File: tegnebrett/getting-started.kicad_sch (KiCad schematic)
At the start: 55 parts, among them J1 FH12-45S-0.5SH55, J2 FH12-6S-1SH55, J3 Conn_ST_STDC14, J5 MCU_Header_Pin, J7 USB_A, SW1 SW_Push, SW2 SW_Push, SW3 SW_Push, SW4 SW_Push, SW5 SW_Push, SW6 SW_Push, SW7 SW_Push, SW8 SW_Push, SW9 SW_Push, U5 STM32U5G7VJTxQ, Y1 60MHz

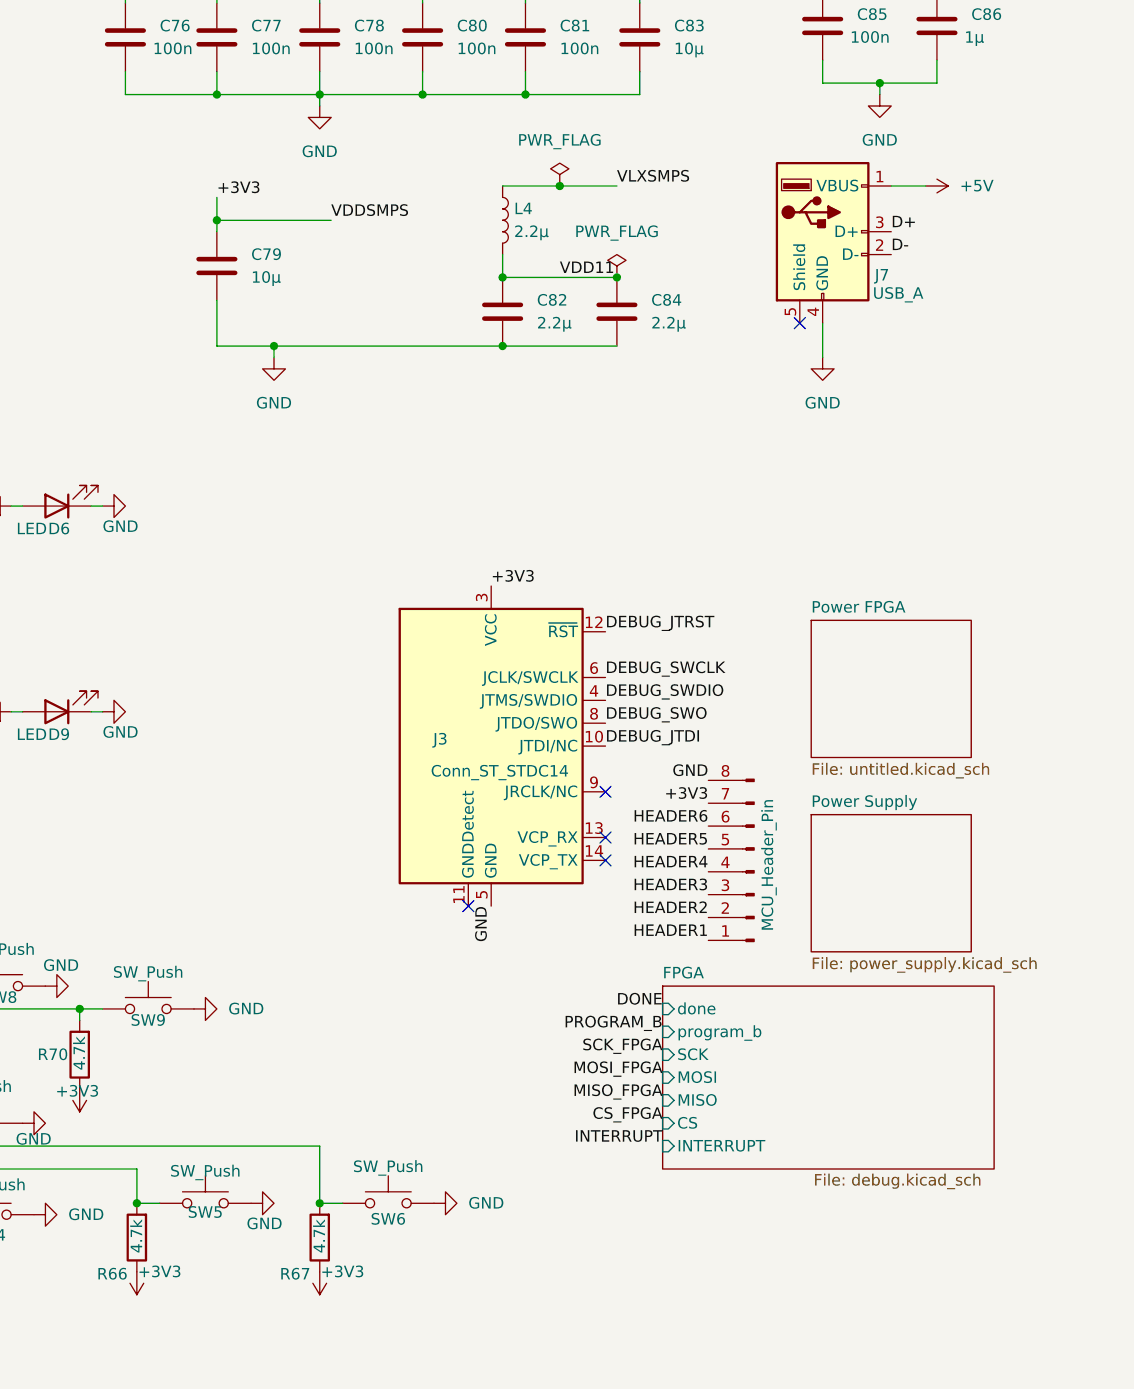
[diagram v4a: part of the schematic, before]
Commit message: feat: add USB-A symbol and footprint to schematic
Also included the 3D model. Now there's some stuff in the PCB.
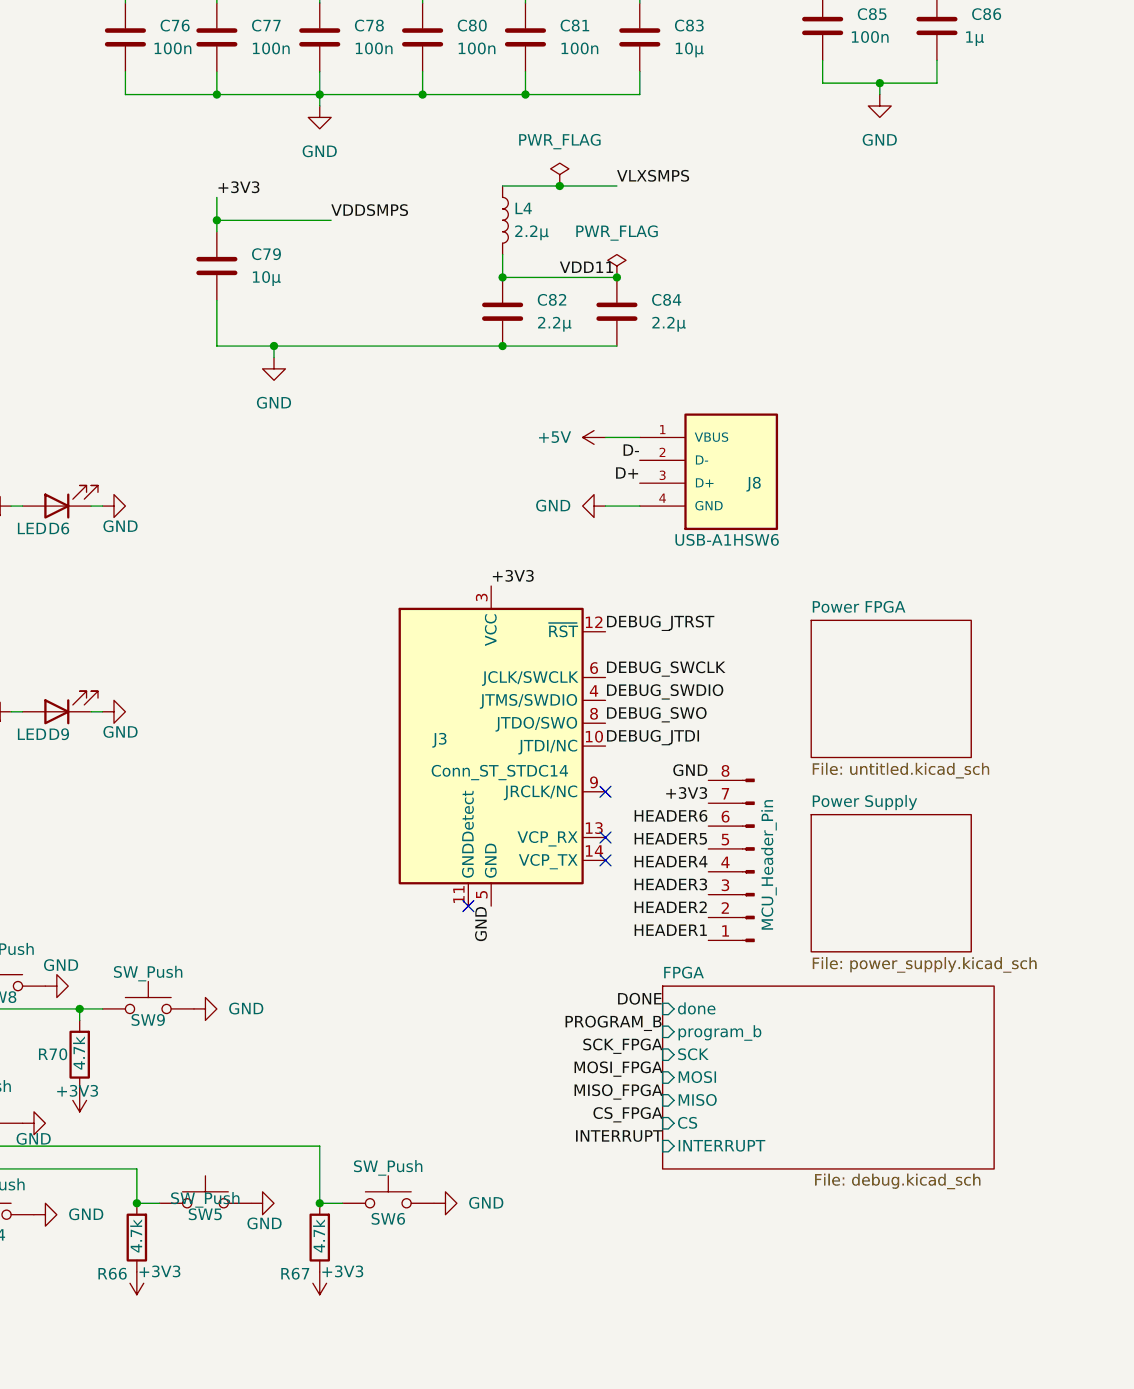
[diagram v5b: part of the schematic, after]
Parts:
- removed J7: USB_A, symbol Connector:USB_A
- added J8: USB-A1HSW6, tegnebrett_modules:OST_USB-A1HSW6, symbol tegnebrett_symbols:USB-A1HSW6
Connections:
- net +5V: now also J8.1 (VBUS)
- net D+: now also J8.3 (D+)
- net D-: now also J8.2 (D-)
- net GND: now also J8.4 (GND)
- no-connect marks 13 -> 12

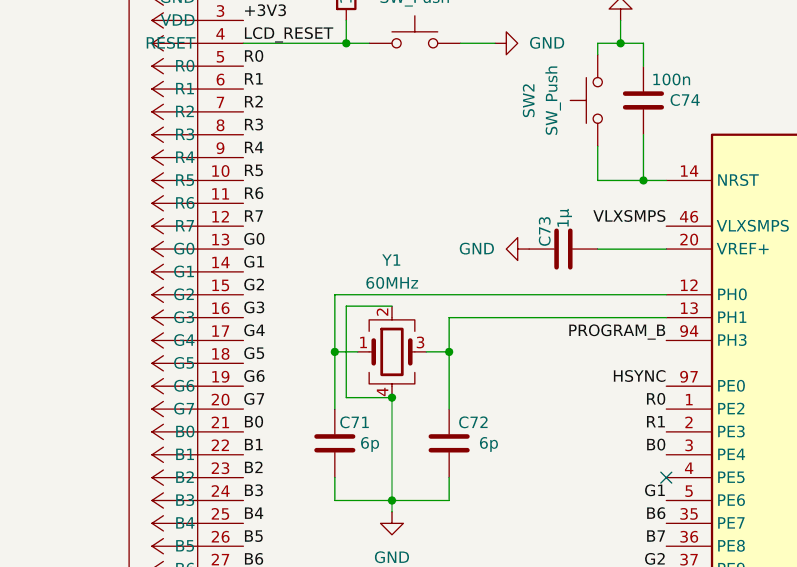
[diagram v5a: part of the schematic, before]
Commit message: feat: add 3d-models to custom footprints
6pin and 45pin, USB-A.
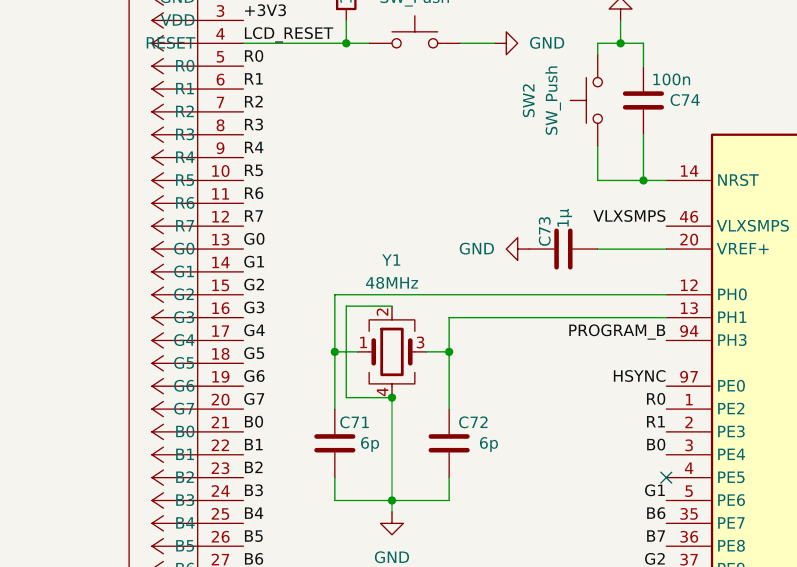
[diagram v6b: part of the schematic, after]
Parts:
- Y1: value 60MHz -> 48MHz
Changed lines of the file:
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@@
 			)
 		)
-		(property "Value" "60MHz"
+		(property "Value" "48MHz"
 			(at 53.34 64.77 0)
 			(effects

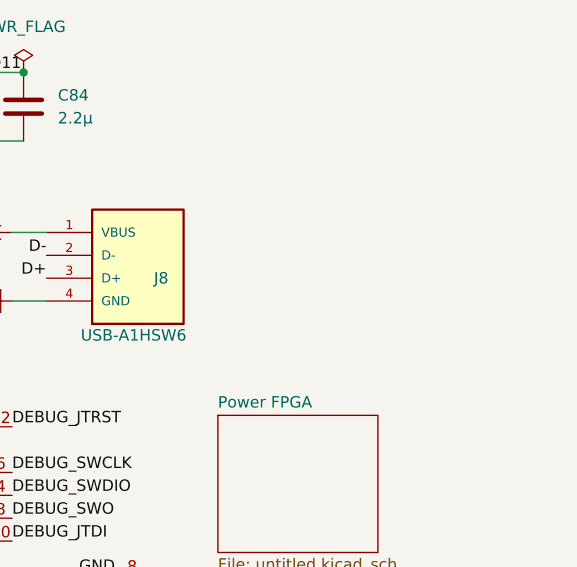
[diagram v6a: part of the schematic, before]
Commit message: feat: add powersupply2
This version supports 5V output.
We need 5V to get USB-A working.
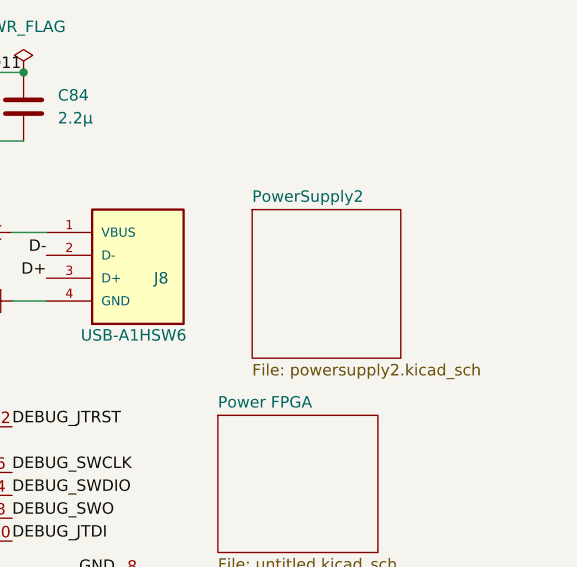
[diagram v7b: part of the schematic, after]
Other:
- added sheet PowerSupply2 (powersupply2.kicad_sch)
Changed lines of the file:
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@@
+	)
+	(sheet
+		(at 266.7 66.04)
+		(size 16.51 16.51)
+		(exclude_from_sim no)
+		(in_bom yes)
+		(on_board yes)
+		(dnp no)
+		(fields_autoplaced yes)
+		(stroke
+			(width 0.1524)
+			(type solid)
+		)
+		(fill
+			(color 0 0 0 0.0000)
+		)
+		(property "Sheetname" "PowerSupply2"
+			(at 266.7 65.3284 0)
+			(effects
+				(font
+					(size 1.27 1.27)
+				)
+				(justify left bottom)
+			)
+		)
+		(property "Sheetfile" "powersupply2.kicad_sch"
+			(at 266.7 83.1346 0)
+			(effects
+				(font
+					(size 1.27 1.27)
+				)
+				(justify left top)
+			)
+		)
+		(instances
+			(project "getting-started"
+				(path "/d9a31669-c5f1-42a7-9461-3df04b9a4e62"
+					(page "6")
+				)
+			)
+		)
 	)
 	(sheet

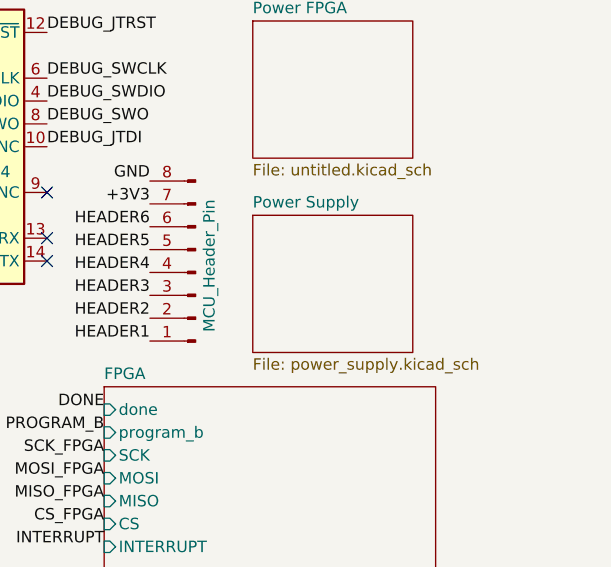
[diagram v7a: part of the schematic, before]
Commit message: feat: remove old power supply schmatic
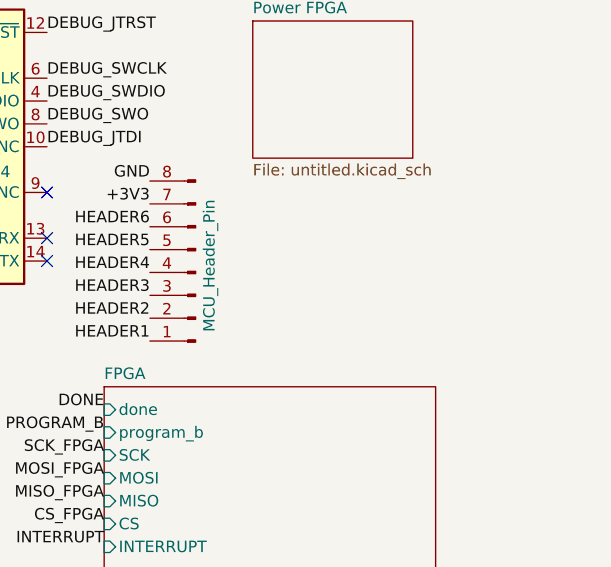
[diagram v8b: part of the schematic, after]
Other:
- removed sheet Power Supply
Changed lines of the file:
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@@
-		)
-	)
-	(sheet
-		(at 262.89 110.49)
-		(size 17.78 15.24)
-		(exclude_from_sim no)
-		(in_bom yes)
-		(on_board yes)
-		(dnp no)
-		(fields_autoplaced yes)
-		(stroke
-			(width 0.1524)
-			(type solid)
-		)
-		(fill
-			(color 0 0 0 0.0000)
-		)
-		(property "Sheetname" "Power Supply"
-			(at 262.89 109.7784 0)
-			(effects
-				(font
-					(size 1.27 1.27)
-				)
-				(justify left bottom)
-			)
-		)
-		(property "Sheetfile" "power_supply.kicad_sch"
-			(at 262.89 126.3146 0)
-			(effects
-				(font
-					(size 1.27 1.27)
-				)
-				(justify left top)
-			)
-		)
-		(instances
-			(project "getting-started"
-				(path "/d9a31669-c5f1-42a7-9461-3df04b9a4e62"
-					(page "6")
-				)
-			)
 		)
 	)
